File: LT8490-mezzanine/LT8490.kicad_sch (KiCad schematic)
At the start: 122 parts, among them J1 Conn_01x01, J10 Conn_01x01, J11 Conn_01x01, J12 Conn_01x01, J13 Conn_01x01, J14 Conn_01x01, J15 Conn_01x01, J16 Conn_01x01, J17 Conn_01x01, J18 Conn_01x01, J19 Conn_01x01, J2 Conn_01x01, J20 Conn_01x01, J21 Conn_01x01, J22 Conn_01x01, J23 Conn_01x01, J24 Conn_01x01, J25 Conn_01x01, J3 Conn_01x01, J4 Conn_01x01, J5 Conn_01x01, J6 Conn_01x01, J7 Conn_01x01, J8 Conn_01x01, J9 Conn_01x01, Q1 SIS128LDN-T1-GE3, Q2 SIS128LDN-T1-GE3, Q3 SIS128LDN-T1-GE3, Q4 SIS128LDN-T1-GE3, Q5 BSS138DWQ-7, Q6 MBT2222ADW1T1, U4 LT8491IUKJPBF

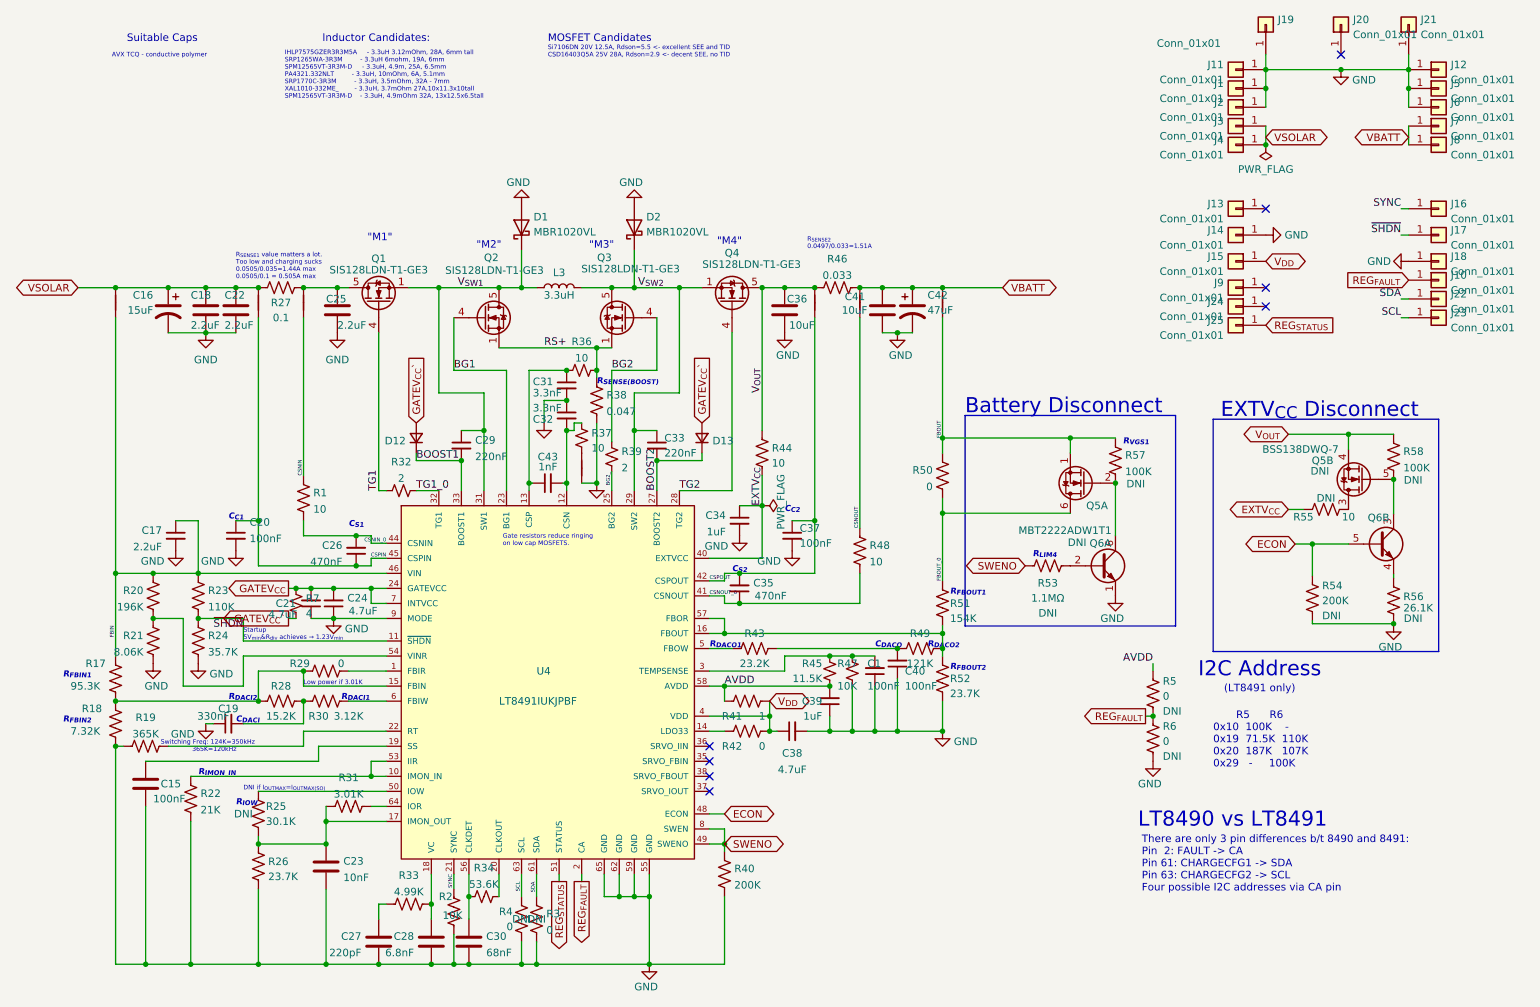
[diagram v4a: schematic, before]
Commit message: cleaned up ibom, fixed transistor footprints, component values
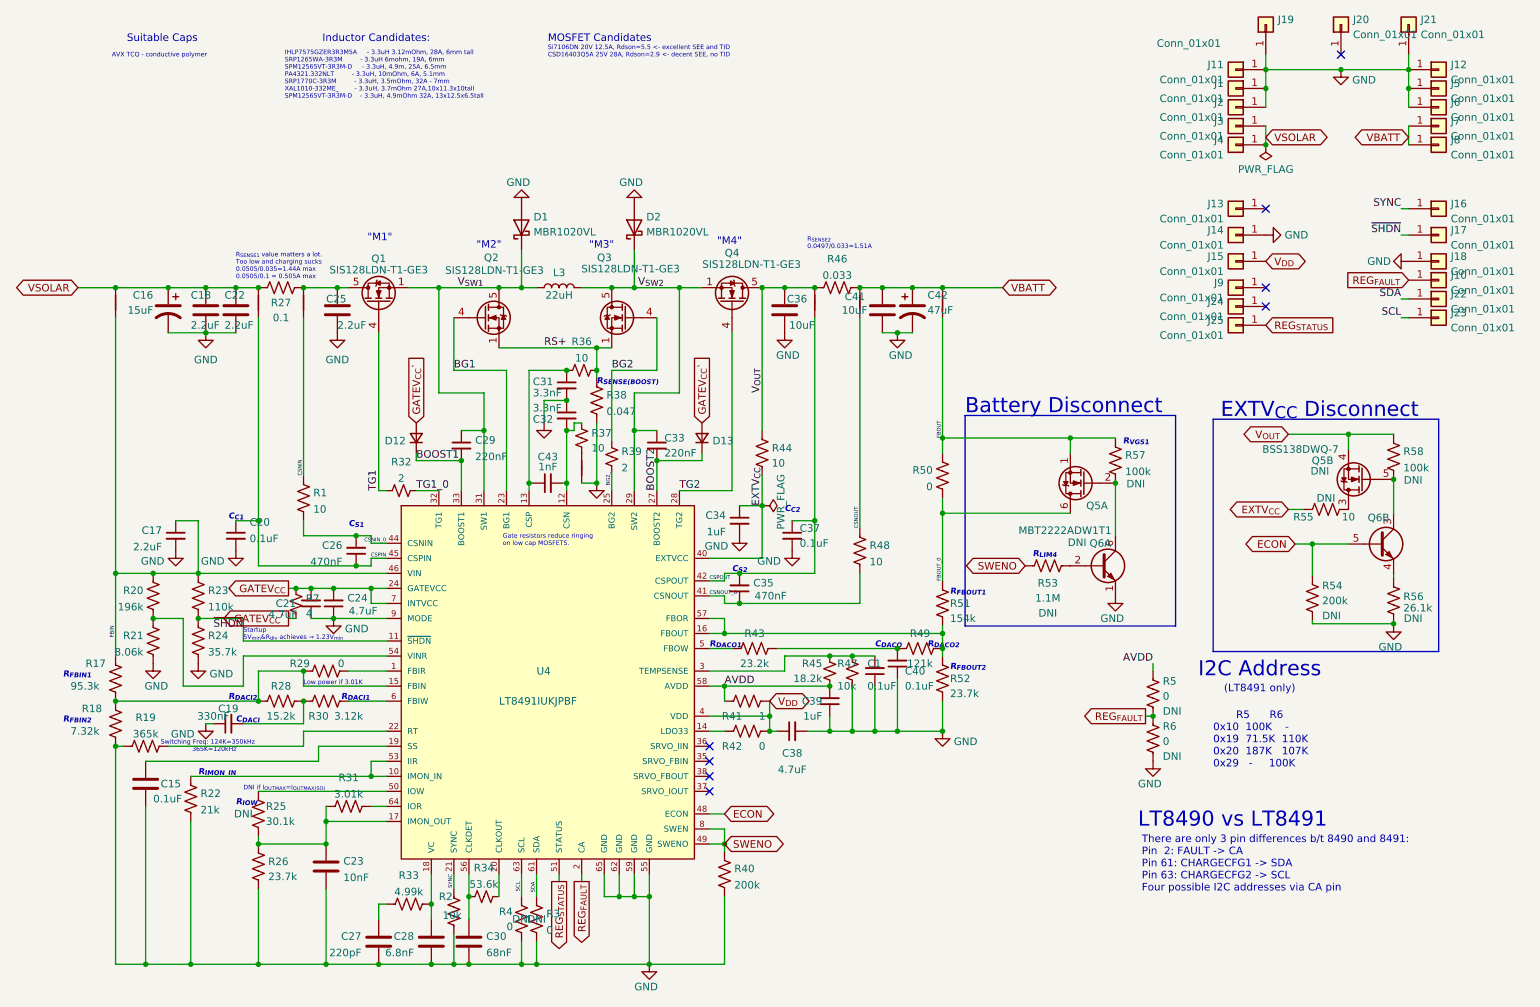
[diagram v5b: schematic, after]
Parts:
- C1, C15, C20, C37, C40: value 100nF -> 0.1uF
- J1, J10, J11, J12, J13, J14, J15, J16, J17, J18, J19, J2, J20, J21, J22, J23, J24, J25, J3, J4, J5, J6, J7, J8, J9: now left out of the parts list
- L3: value 3.3uH -> 22uH
- R17: value 95.3K -> 95.3k
- R18: value 7.32K -> 7.32k
- R19: value 365K -> 365k
- R2, R47: value 10K -> 10k
- R20: value 196K -> 196k
- R21: value 8.06K -> 8.06k
- R22: value 21K -> 21k
- R23: value 110K -> 110k
- R24: value 35.7K -> 35.7k
- R25: value 30.1K -> 30.1k
- R26, R52: value 23.7K -> 23.7k
- R28: value 15.2K -> 15.2k
- R30: value 3.12K -> 3.12k
- R31: value 3.01K -> 3.01k
- R33: value 4.99K -> 4.99k
- R34: value 53.6K -> 53.6k
- R40, R54: value 200K -> 200k
- R43: value 23.2K -> 23.2k
- R45: value 11.5K -> 18.2k
- R49: value 121K -> 121k
- R51: value 154K -> 154k
- R53: value 1.1MΩ -> 1.1M
- R56: value 26.1K -> 26.1k
- R57, R58: value 100K -> 100k
